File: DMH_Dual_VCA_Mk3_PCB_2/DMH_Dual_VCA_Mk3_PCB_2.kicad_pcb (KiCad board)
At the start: 2 copper layers, 48 x 120.5 mm, 11 parts, among them J0 Conn_01x01, J50 Conn_01x08, J60 Conn_01x08

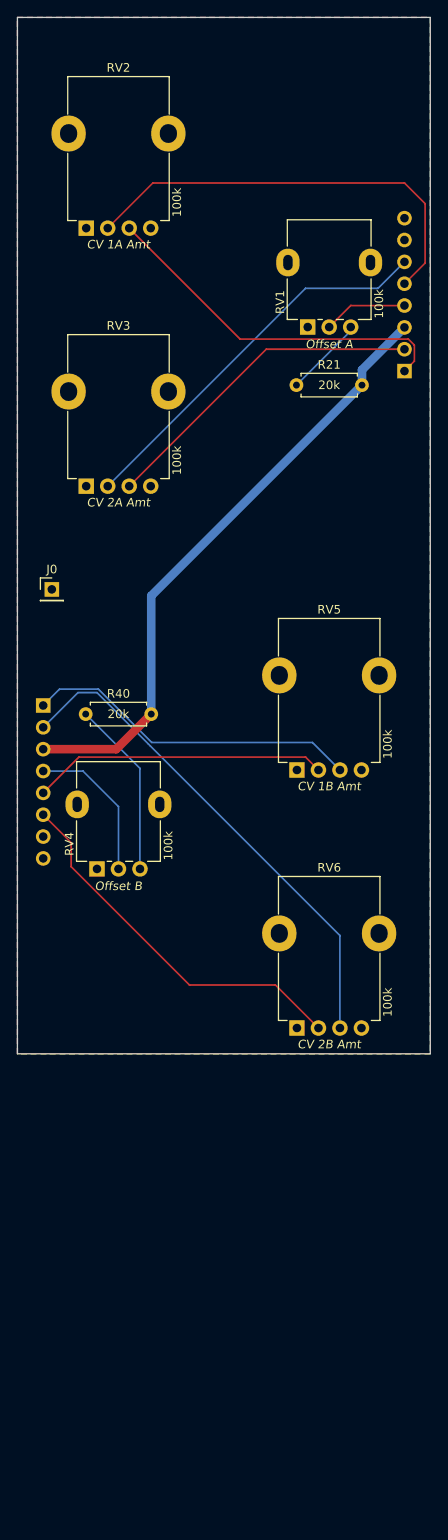
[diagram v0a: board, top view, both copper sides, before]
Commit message: Synced PCB 1 and 2 schematics
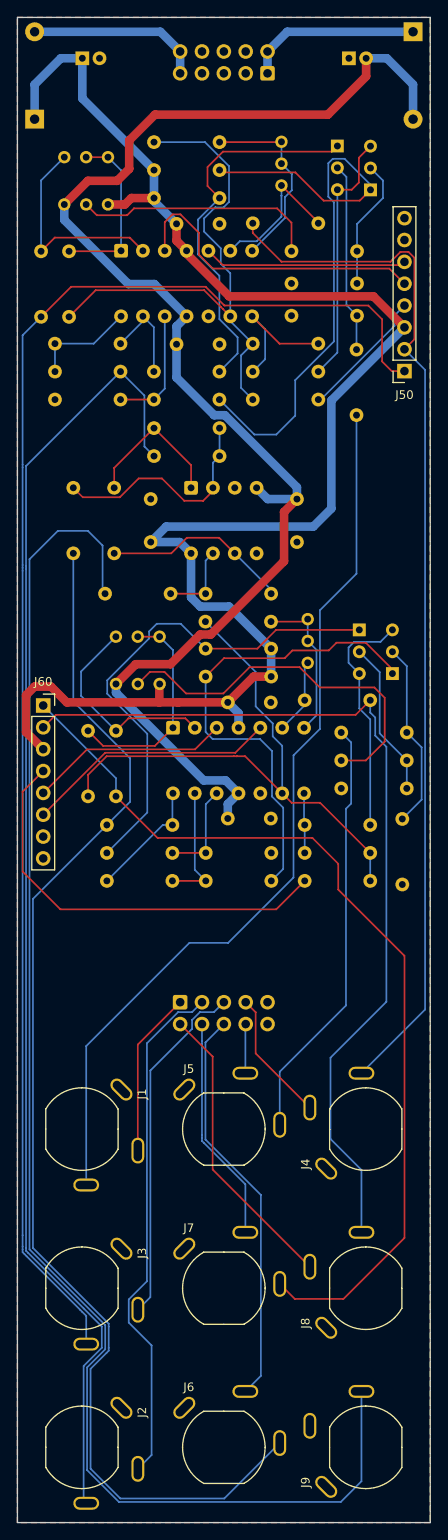
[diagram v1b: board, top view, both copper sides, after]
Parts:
- removed J0: Conn_01x01, Connector_PinHeader_2.54mm:PinHeader_1x01_P2.54mm_Vertical
- removed R21, R40: 20k, Resistor_THT:R_Axial_DIN0207_L6.3mm_D2.5mm_P7.62mm_Horizontal
- removed RV1, RV4: 100k, SynthStuff:Potentiometer_Alpha_RD901F-40-00D_Single_Vertical
- removed RV2, RV3, RV5, RV6: 100k, SynthStuff:Potentiometer_TT_P110KH1
- added C1: 47uF, Capacitor_THT:CP_Radial_D5.0mm_P2.00mm, B.Cu at (58.5, 47.2)
- added C2: 47uF, Capacitor_THT:CP_Radial_D5.0mm_P2.00mm, B.Cu at (89.5, 47.2)
- added C3: 100nF, Capacitor_THT:C_Disc_D4.3mm_W1.9mm_P5.00mm, B.Cu at (69.5, 66.5)
- added C4: 100nF, Capacitor_THT:C_Disc_D4.3mm_W1.9mm_P5.00mm, B.Cu at (74.5, 80.5)
- added C5: 100nF, Capacitor_THT:C_Disc_D4.3mm_W1.9mm_P5.00mm, B.Cu at (75.5, 122.1)
- added C6: 100nF, Capacitor_THT:C_Disc_D4.3mm_W1.9mm_P5.00mm, B.Cu at (80.5, 135.6)
- added C7: 100nF, Capacitor_THT:C_Disc_D4.3mm_W1.9mm_P5.00mm, B.Cu at (66.5, 103.5)
- added C8: 100nF, Capacitor_THT:C_Disc_D4.3mm_W1.9mm_P5.00mm, B.Cu at (83.5, 103.5)
- added D1: SB140+, Diode_THT:D_DO-41_SOD81_P10.16mm_Horizontal, B.Cu at (53.0, 54.3)
- added D2: SB140-, Diode_THT:D_DO-41_SOD81_P10.16mm_Horizontal, B.Cu at (97.0, 44.2)
- added J1: TS_Jack_6.35mm_Sw, SynthStuff:CUI_MJ-63052A, F.Cu at (58.5, 171.8)
- added J100: IDC_02x05, SynthStuff:IDC-Header_2x05_P2.54mm_Vertical_Eurorack, B.Cu at (80.1, 49.0)
- added J2: TS_Jack_6.35mm_Sw, SynthStuff:CUI_MJ-63052A, F.Cu at (58.5, 208.8)
- added J200: IDC_02x05, SynthStuff:IDC-Header_2x05_P2.54mm_Vertical_BackBone, B.Cu at (69.9, 157.0)
- added J3: TS_Jack_6.35mm_Sw, SynthStuff:CUI_MJ-63052A, F.Cu at (58.5, 190.2)
- added J4: TS_Jack_6.35mm_Sw, SynthStuff:CUI_MJ-63052A, F.Cu at (91.5, 171.8)
- added J5: TS_Jack_6.35mm_Sw, SynthStuff:CUI_MJ-63052A, F.Cu at (75.0, 171.8)
- added J6: TS_Jack_6.35mm_Sw, SynthStuff:CUI_MJ-63052A, F.Cu at (75.0, 208.8)
- added J7: TS_Jack_6.35mm_Sw, SynthStuff:CUI_MJ-63052A, F.Cu at (75.0, 190.2)
- added J8: TS_Jack_6.35mm_Sw, SynthStuff:CUI_MJ-63052A, F.Cu at (91.5, 190.2)
- added J9: TS_Jack_6.35mm_Sw, SynthStuff:CUI_MJ-63052A, F.Cu at (91.5, 208.8)
- added Q1: BC548, Package_TO_SOT_THT:TO-92L_Inline_Wide, B.Cu at (88.2, 57.5)
- added Q2: BC548, Package_TO_SOT_THT:TO-92L_Inline_Wide, B.Cu at (92.0, 62.5)
- added Q3: BC548, Package_TO_SOT_THT:TO-92L_Inline_Wide, B.Cu at (94.6, 118.8)
- added Q4: BC548, Package_TO_SOT_THT:TO-92L_Inline_Wide, B.Cu at (90.8, 113.7)
- added R1: 33k, Resistor_THT:R_Axial_DIN0207_L6.3mm_D2.5mm_P7.62mm_Horizontal, B.Cu at (53.8, 77.3)
- added R10: 100R, Resistor_THT:R_Axial_DIN0207_L6.3mm_D2.5mm_P7.62mm_Horizontal, B.Cu at (82.9, 77.2)
- added R11: 100k, Resistor_THT:R_Axial_DIN0207_L6.3mm_D2.5mm_P7.62mm_Horizontal, B.Cu at (90.4, 81.1)
- added R12: 100k, Resistor_THT:R_Axial_DIN0207_L6.3mm_D2.5mm_P7.62mm_Horizontal, B.Cu at (82.9, 69.7)
- added R13: 100R, Resistor_THT:R_Axial_DIN0207_L6.3mm_D2.5mm_P7.62mm_Horizontal, B.Cu at (82.9, 73.4)
- added R14: 20k, Resistor_THT:R_Axial_DIN0207_L6.3mm_D2.5mm_P7.62mm_Horizontal, B.Cu at (74.5, 63.5)
- added R15: 20k, Resistor_THT:R_Axial_DIN0207_L6.3mm_D2.5mm_P7.62mm_Horizontal, B.Cu at (74.5, 60.2)
- added R16: 10k, Resistor_THT:R_Axial_DIN0207_L6.3mm_D2.5mm_P7.62mm_Horizontal, B.Cu at (66.9, 83.7)
- added R17: 10k, Resistor_THT:R_Axial_DIN0207_L6.3mm_D2.5mm_P7.62mm_Horizontal, B.Cu at (66.9, 86.9)
- added R18: 100k, Resistor_THT:R_Axial_DIN0207_L6.3mm_D2.5mm_P7.62mm_Horizontal, B.Cu at (55.4, 80.4)
- added R19: 100k, Resistor_THT:R_Axial_DIN0207_L6.3mm_D2.5mm_P7.62mm_Horizontal, B.Cu at (63.0, 86.9)
- added R20: 1k, Resistor_THT:R_Axial_DIN0207_L6.3mm_D2.5mm_P7.62mm_Horizontal, B.Cu at (63.0, 83.7)
- added R22: 20k, Resistor_THT:R_Axial_DIN0207_L6.3mm_D2.5mm_P7.62mm_Horizontal, B.Cu at (72.9, 119.1)
- added R23: 20k, Resistor_THT:R_Axial_DIN0207_L6.3mm_D2.5mm_P7.62mm_Horizontal, B.Cu at (72.9, 115.9)
- added R24: 33k, Resistor_THT:R_Axial_DIN0207_L6.3mm_D2.5mm_P7.62mm_Horizontal, B.Cu at (62.5, 133.1)
- added R25: 100k, Resistor_THT:R_Axial_DIN0207_L6.3mm_D2.5mm_P7.62mm_Horizontal, B.Cu at (61.4, 142.9)
- added R26: 10k, Resistor_THT:R_Axial_DIN0207_L6.3mm_D2.5mm_P7.62mm_Horizontal, B.Cu at (72.9, 142.9)
- added R28: 100k, Resistor_THT:R_Axial_DIN0207_L6.3mm_D2.5mm_P7.62mm_Horizontal, B.Cu at (59.2, 125.4)
- added R29: 1k, Resistor_THT:R_Axial_DIN0207_L6.3mm_D2.5mm_P7.62mm_Horizontal, B.Cu at (61.4, 136.4)
- added R3: 100k, Resistor_THT:R_Axial_DIN0207_L6.3mm_D2.5mm_P7.62mm_Horizontal, B.Cu at (57.0, 69.7)
- added R30: 10k, Resistor_THT:R_Axial_DIN0207_L6.3mm_D2.5mm_P7.62mm_Horizontal, B.Cu at (69.0, 139.6)
- added R31: 100k, Resistor_THT:R_Axial_DIN0207_L6.3mm_D2.5mm_P7.62mm_Horizontal, B.Cu at (72.9, 139.6)
- added R32: 33k, Resistor_THT:R_Axial_DIN0207_L6.3mm_D2.5mm_P7.62mm_Horizontal, B.Cu at (92.0, 121.9)
- added R33: 100k, Resistor_THT:R_Axial_DIN0207_L6.3mm_D2.5mm_P7.62mm_Horizontal, B.Cu at (96.3, 125.6)
- added R34: 100k, Resistor_THT:R_Axial_DIN0207_L6.3mm_D2.5mm_P7.62mm_Horizontal, B.Cu at (88.7, 128.9)
- added R35: 100R, Resistor_THT:R_Axial_DIN0207_L6.3mm_D2.5mm_P7.62mm_Horizontal, B.Cu at (95.8, 143.3)
- added R36: 100R, Resistor_THT:R_Axial_DIN0207_L6.3mm_D2.5mm_P7.62mm_Horizontal, B.Cu at (88.7, 132.1)
- added R38: 100k, Resistor_THT:R_Axial_DIN0207_L6.3mm_D2.5mm_P7.62mm_Horizontal, B.Cu at (80.5, 112.8)
- added R39: 10k, Resistor_THT:R_Axial_DIN0207_L6.3mm_D2.5mm_P7.62mm_Horizontal, B.Cu at (84.4, 136.4)
- added R4: 33k, Resistor_THT:R_Axial_DIN0207_L6.3mm_D2.5mm_P7.62mm_Horizontal, B.Cu at (78.4, 66.4)
- added R41: 100k, Resistor_THT:R_Axial_DIN0207_L6.3mm_D2.5mm_P7.62mm_Horizontal, B.Cu at (92.0, 139.6)
- added R42: 100k, Resistor_THT:R_Axial_DIN0207_L6.3mm_D2.5mm_P7.62mm_Horizontal, B.Cu at (84.4, 142.9)
- added R46: 100k, Resistor_THT:R_Axial_DIN0207_L6.3mm_D2.5mm_P7.62mm_Horizontal, B.Cu at (57.5, 104.8)
- added R47: 100k, Resistor_THT:R_Axial_DIN0207_L6.3mm_D2.5mm_P7.62mm_Horizontal, B.Cu at (74.5, 90.2)
- added R48: 100k, Resistor_THT:R_Axial_DIN0207_L6.3mm_D2.5mm_P7.62mm_Horizontal, B.Cu at (66.9, 93.5)
- added R49: 100k, Resistor_THT:R_Axial_DIN0207_L6.3mm_D2.5mm_P7.62mm_Horizontal, B.Cu at (62.2, 97.2)
- added R50: 100k, Resistor_THT:R_Axial_DIN0207_L6.3mm_D2.5mm_P7.62mm_Horizontal, B.Cu at (80.5, 109.5)
- added R51: 1k, Resistor_THT:R_Axial_DIN0207_L6.3mm_D2.5mm_P7.62mm_Horizontal, B.Cu at (68.8, 109.5)
- added R6: 100k, Resistor_THT:R_Axial_DIN0207_L6.3mm_D2.5mm_P7.62mm_Horizontal, B.Cu at (74.5, 57.0)
- added R7: 100k, Resistor_THT:R_Axial_DIN0207_L6.3mm_D2.5mm_P7.62mm_Horizontal, B.Cu at (86.0, 86.9)
- added R8: 100k, Resistor_THT:R_Axial_DIN0207_L6.3mm_D2.5mm_P7.62mm_Horizontal, B.Cu at (78.4, 80.4)
- added R9: 10k, Resistor_THT:R_Axial_DIN0207_L6.3mm_D2.5mm_P7.62mm_Horizontal, B.Cu at (78.4, 83.7)
- added RV10: 50k, Potentiometer_THT:Potentiometer_Bourns_3296W_Vertical, B.Cu at (81.7, 62.0)
- added RV11: 50k, Potentiometer_THT:Potentiometer_Bourns_3296W_Vertical, B.Cu at (62.5, 114.5)
- added RV12: 50k, Potentiometer_THT:Potentiometer_Bourns_3296W_Vertical, B.Cu at (84.8, 117.5)
- added RV7: 100k, Potentiometer_THT:Potentiometer_Bourns_3296W_Vertical, B.Cu at (56.5, 64.2)
- added RV8: 100k, Potentiometer_THT:Potentiometer_Bourns_3296W_Vertical, B.Cu at (62.5, 120.0)
- added RV9: 50k, Potentiometer_THT:Potentiometer_Bourns_3296W_Vertical, B.Cu at (56.5, 58.8)
- added U1: TL074, Package_DIP:DIP-14_W7.62mm_Socket, B.Cu at (63.0, 69.6)
- added U2: TL074, Package_DIP:DIP-14_W7.62mm_Socket, B.Cu at (69.1, 125.1)
- added U3: TL072, Package_DIP:DIP-8_W7.62mm_Socket, B.Cu at (71.2, 97.2)
- J50, J60: footprint Connector_PinHeader_2.54mm:PinHeader_1x08_P2.54mm_Vertical -> Connector_PinSocket_2.54mm:PinSocket_1x08_P2.54mm_Vertical; moved to F.Cu
- turned J50 to 180 degrees
- turned J60 to 0 degrees
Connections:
- J50 pad 1: /Inputs and Outputs/CV 1 A Jack -> /Core Circuit A/CV 1 A Input
- J50 pad 2: /Inputs and Outputs/CV 2 A Jack -> /Core Circuit A/CV 2 A Input
- J50 pad 4: /Inputs and Outputs/Offset A Pot -> /Core Circuit A/Offset A Pot
- J50 pad 5: /Inputs and Outputs/CV 1 A Pot -> /Core Circuit A/CV 1 A Pot
- J50 pad 6: /Inputs and Outputs/CV 2 A Pot -> /Core Circuit A/CV 2 A Pot
- J60 pad 1: /Inputs and Outputs/CV 1 B Jack -> /Core Circuit B/CV 1 B Input
- J60 pad 2: /Inputs and Outputs/CV 2 B Jack -> /Core Circuit B/CV 2 B Input
- J60 pad 4: /Inputs and Outputs/Offset B Pot -> /Core Circuit B/Offset B Pot
- J60 pad 5: /Inputs and Outputs/CV 1 B Pot -> /Core Circuit B/CV 1 B Pot
- J60 pad 6: /Inputs and Outputs/CV 2 B Pot -> /Core Circuit B/CV 2 B Pot
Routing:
- net /Core Circuit A/CV 1 A Input: track 0.00 -> 174.0 mm
- net /Inputs and Outputs/Mix Out Jack: track 0.00 -> 171.6 mm
- net -12V: track 0.00 -> 167.1 mm
- net /Core Circuit A/Output A: track 0.00 -> 152.2 mm
- net /Core Circuit B/Output B: track 0.00 -> 144.5 mm
- net /Core Circuit A/CV 2 A Input: track 0.00 -> 121.4 mm
- net +12V: track 71.4 -> 189.3 mm
- net /Core Circuit B/CV 1 B Input: track 0.00 -> 108.0 mm
- net /Core Circuit B/CV 2 B Input: track 0.00 -> 106.1 mm
- net /Core Circuit A/Input A: track 0.00 -> 105.2 mm
- net Net-(Q2-C): track 0.00 -> 69.4 mm
- net Net-(U2C--): track 0.00 -> 67.8 mm
- net Net-(U1C--): track 0.00 -> 63.6 mm
- net Net-(J200-Pin_2): track 0.00 -> 60.5 mm
- net /Inputs and Outputs/CV 2 B Jack: track 58.6 -> 0.00 mm
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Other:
- board size 48 x 120.5 mm -> 48 x 175 mm
